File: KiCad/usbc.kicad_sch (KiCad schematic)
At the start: 26 parts, among them J26 JACK-USBE-20PINTL, U18 ZD25Q64BSIGT, U19 TPS65987DDJRSHR, U43 H5VU25U, U44 H5VU25U

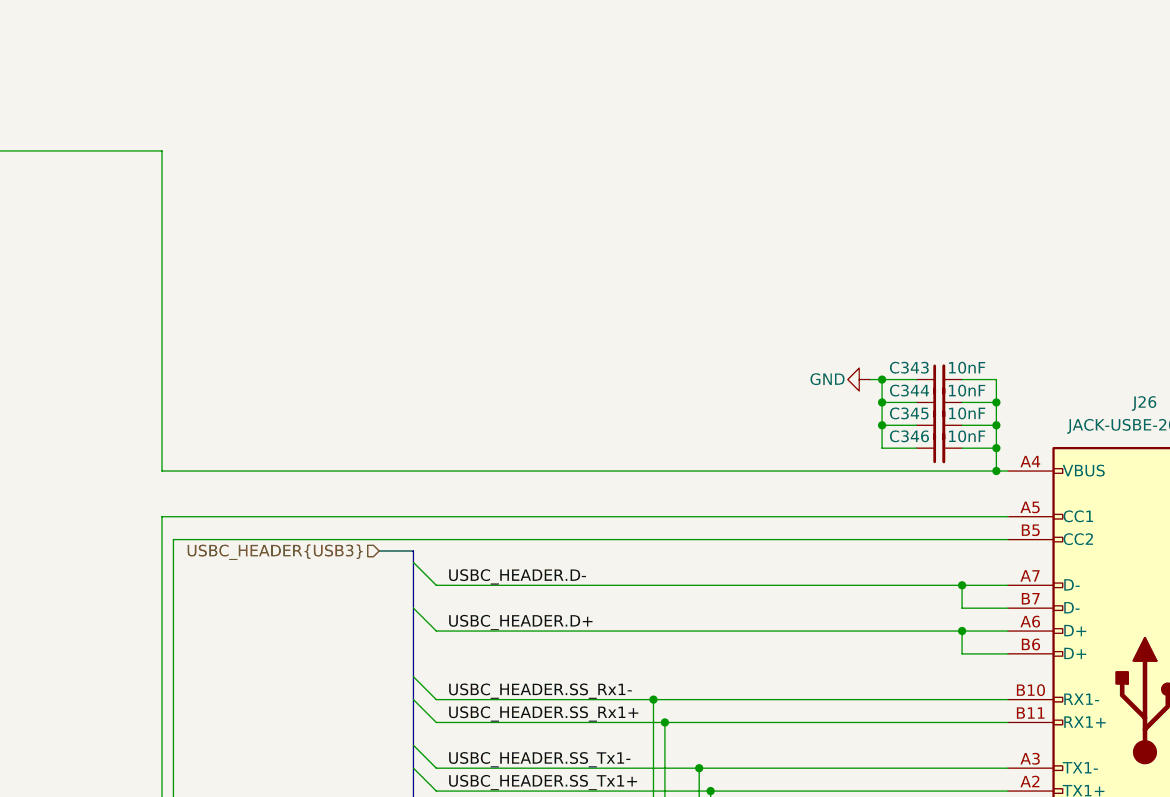
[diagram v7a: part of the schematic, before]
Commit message: Fix esd diodes, add some footprints.
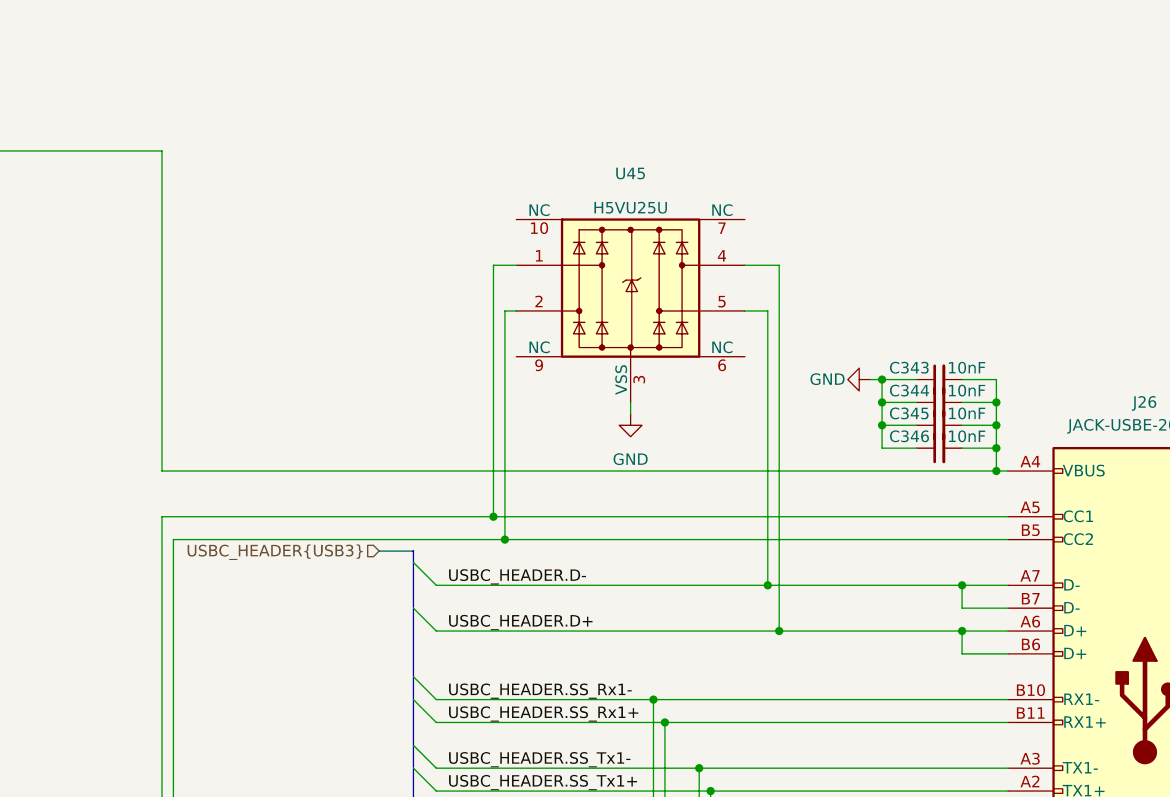
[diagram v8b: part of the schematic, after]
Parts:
- added U45: H5VU25U, Package_DFN_QFN:Diodes_UDFN-10_1.0x2.5mm_P0.5mm, symbol Power_Protection:D3V3XA4B10LP
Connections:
- net GND: now also U45.3 (VSS), U45.8 (VSS)
- net USBC_HEADER.D+: now also U45.4
- net USBC_HEADER.D-: now also U45.5
- net at C341.1, J26.A5 (CC1), U19.24 (C_CC1): now also U45.1
- net at C342.1, J26.B5 (CC2), U19.26 (C_CC2): now also U45.2
